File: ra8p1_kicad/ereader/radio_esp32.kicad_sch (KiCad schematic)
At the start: 28 parts, among them U3 ESP32-C6-WROOM-1-N8, U4 TPS22917DBVT, U5 TXU0304PWR, U6 TPS389001DSET, U7 SN74LVC1G97DBVR, U8 SN74LVC1G97DBVR

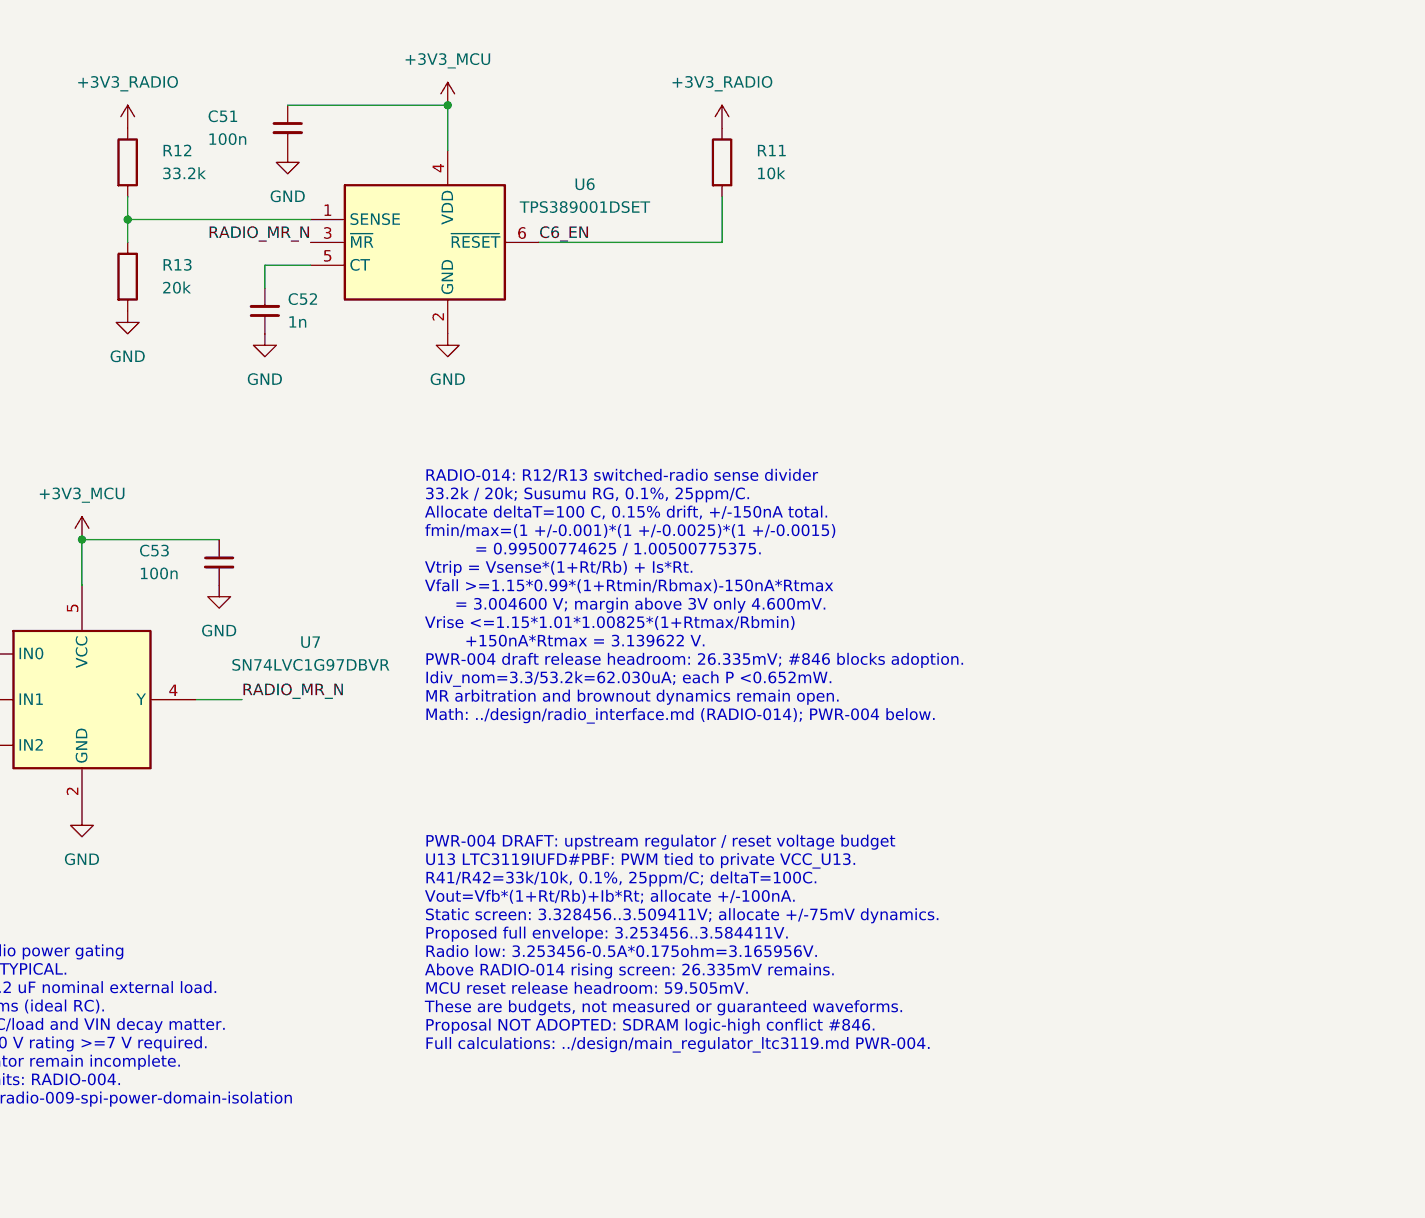
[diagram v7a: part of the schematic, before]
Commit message: Complete MCU reset checkpoint and portable engineering records
Refs #825, #826, #846. Preserve the unresolved radio release margin and unfinished schematic status; refresh full PDF and native BOM.
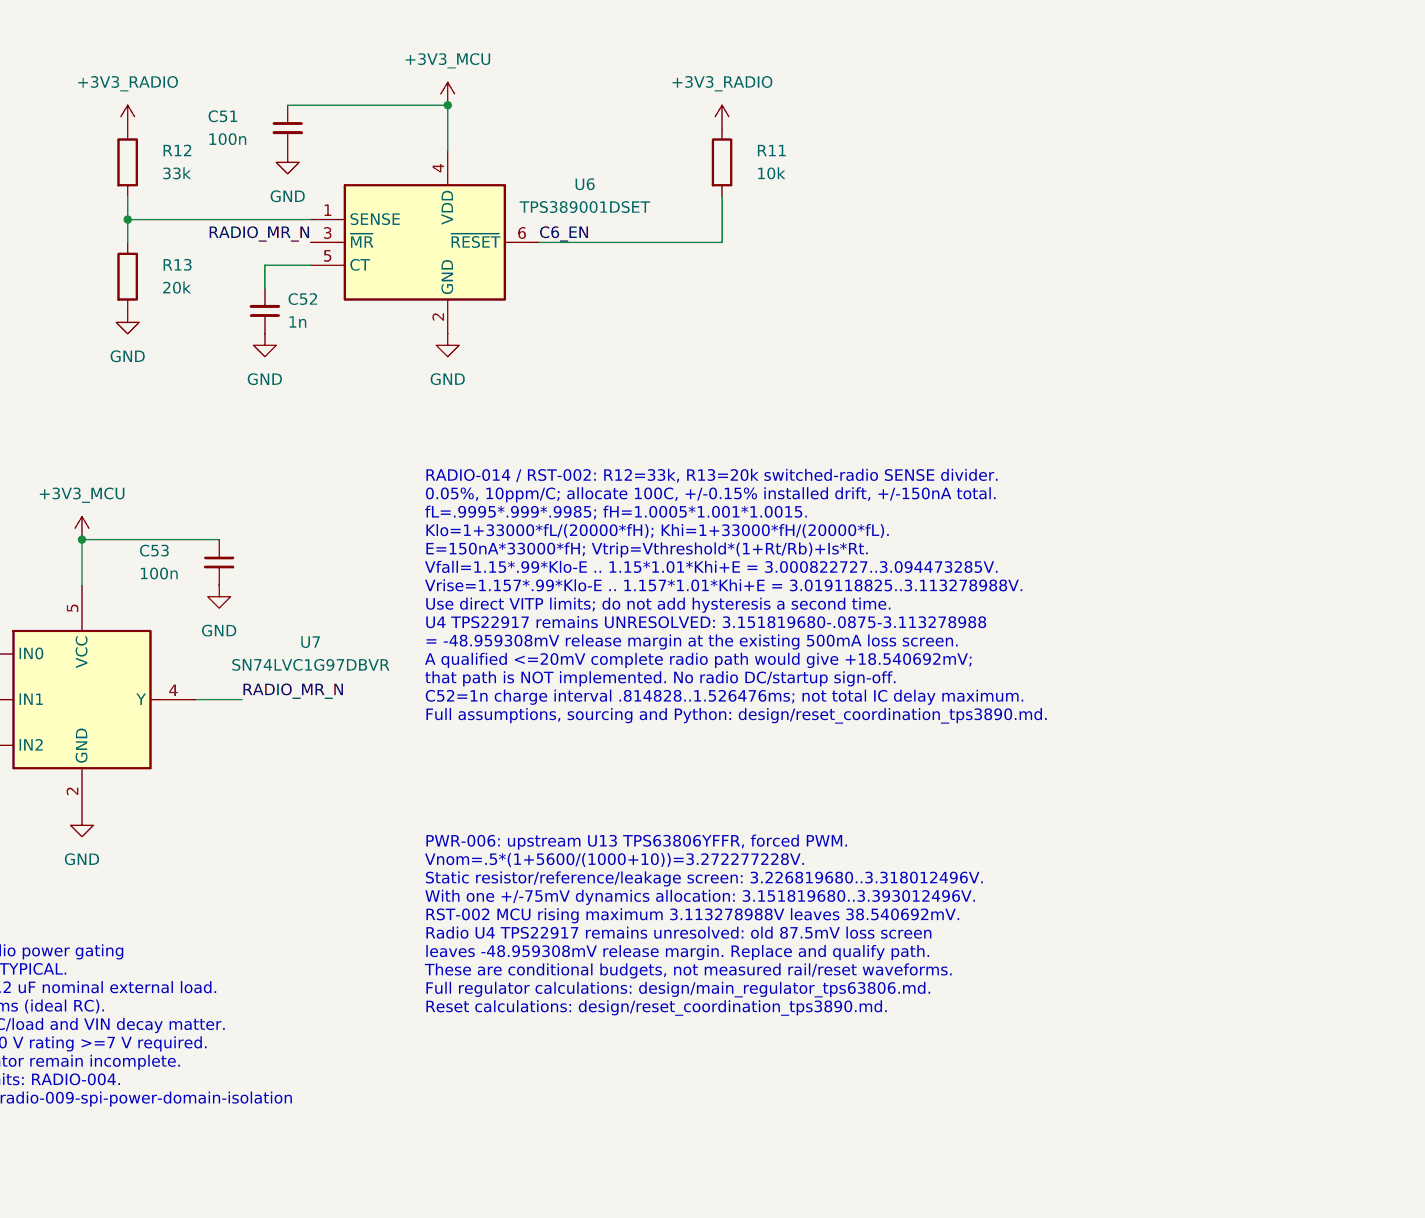
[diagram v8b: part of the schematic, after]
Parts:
- R12: value 33.2k -> 33k; DigiKey_Part_Number RG16P33.2KBCT-ND -> P33KBSCT-ND; DigiKey_URL https://www.digikey.com/en/products/detail/susumu/RG1608P-3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 -> https://www.digikey.com/en/products/detail/panasonic-indust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; Manufacturer_Name Susumu -> Panasonic Industry; Manufacturer_Part_Number RG1608P-3322-B-T5 -> ERA-6ARW333V; Procurement_Status Selected - electrical ratings and sourcing checked; footpri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 -> Selected; installed drift and reset qualification required;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; Selection_Basis RADIO-014 upper divider: 33.2k/20k, 0.1% 25ppm/C. Include 1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 -> RST-002: 33k upper SENSE with 20k lower; 0.05%, 10ppm/C. Co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; Sourcing_Snapshot 2026-09-07 indexed: Active; stock 95362; USD CT 1:0.13 / 10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 -> 2026-09-08 DigiKey cut tape: 9330 stock; USD0.57/0.472/0.39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
- R13: DigiKey_Part_Number RG16P20.0KBCT-ND -> RG16N20.0KWCT-ND; DigiKey_URL https://www.digikey.com/en/products/detail/susumu/RG1608P-2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 -> https://www.digikey.com/en/products/detail/susumu/RG1608N-2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; Manufacturer_Part_Number RG1608P-203-B-T5 -> RG1608N-203-W-T1; Procurement_Status Selected - electrical ratings and sourcing checked; footpri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 -> Selected; installed drift and reset qualification required;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; Selection_Basis RADIO-014 lower divider: 33.2k/20k, 0.1% 25ppm/C. Include 1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 -> RST-002: 20k lower SENSE with 33k upper; 0.05%, 10ppm/C. Co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; Sourcing_Snapshot 2026-09-07 indexed: Active; stock 186950; USD CT 1:0.11 / 1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 -> 2026-09-08 DigiKey cut tape: 78737 stock; USD0.64/0.529/0.4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
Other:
- note added: "PWR-006: upstream U13 TPS63806YFFR, forced PWM. Vnom=.5*(1+5600/(1000+10))=3.272277228V. Static resistor/reference/leakage screen: 3.226819680..3.318012496V. With one +/-75mV dynamics allocation: 3.151819680..3.393012496V. RST-002 MCU rising maximum 3.113278988V leaves 38.540692mV. Radio U4 TPS22917 remains unresolved: old 87.5mV loss screen leaves -48.959308mV release margin. Replace and qualify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"
- note added: "RADIO-014 / RST-002: R12=33k, R13=20k switched-radio SENSE divider. 0.05%, 10ppm/C; allocate 100C, +/-0.15% installed drift, +/-150nA total. fL=.9995*.999*.9985; fH=1.0005*1.001*1.0015. Klo=1+33000*fL/(20000*fH); Khi=1+33000*fH/(20000*fL). E=150nA*33000*fH; Vtrip=Vthreshold*(1+Rt/Rb)+Is*Rt. Vfall=1.15*.99*Klo-E .. 1.15*1.01*Khi+E = 3.000822727..3.094473285V. Vrise=1.157*.99*Klo-E .. 1.157*1.01*Kh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"
- note removed: "PWR-004 DRAFT: upstream regulator / reset voltage budget U13 LTC3119IUFD#PBF: PWM tied to private VCC_U13. R41/R42=33k/10k, 0.1%, 25ppm/C; deltaT=100C. Vout=Vfb*(1+Rt/Rb)+Ib*Rt; allocate +/-100nA. Static screen: 3.328456..3.509411V; allocate +/-75mV dynamics. Proposed full envelope: 3.253456..3.584411V. Radio low: 3.253456-0.5A*0.175ohm=3.165956V. Above RADIO-014 rising screen: 26.335mV remains. 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"
- note removed: "RADIO-014: R12/R13 switched-radio sense divider 33.2k / 20k; Susumu RG, 0.1%, 25ppm/C. Allocate deltaT=100 C, 0.15% drift, +/-150nA total. fmin/max=(1 +/-0.001)*(1 +/-0.0025)*(1 +/-0.0015) = 0.99500774625 / 1.00500775375. Vtrip = Vsense*(1+Rt/Rb) + Is*Rt. Vfall >=1.15*0.99*(1+Rtmin/Rbmax)-150nA*Rtmax = 3.004600 V; margin above 3V only 4.600mV. Vrise <=1.15*1.01*1.00825*(1+Rtmax/Rbmin) +150nA*Rtma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"
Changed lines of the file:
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@@
 		(comment 1 "Incomplete electrical design - not for manufacture")
 	)
-	(text "PWR-004 DRAFT: upstream regulator / reset voltage budget\nU13 LTC3119IUFD#PBF: PWM tied to private VCC_U13.\nR41/R42=33k/10k, 0.1%, 25ppm/C; deltaT=100C.\nVout=Vfb*(1+Rt/Rb)+Ib*Rt; allocate +/-100nA.\nStatic screen: 3.328456..3.509411V; allocate +/-75mV dynamics.\nProposed full envelope: 3.253456..3.584411V.\nRadio low: 3.253456-0.5A*0.175ohm=3.165956V.\nAbove RADIO-014 rising screen: 26.335mV remains.\nMCU reset release headroom: 59.505mV.\nThese are budgets, not measured or guaranteed waveforms.\nProposal NOT ADOPTED: SDRAM logic-high conflict #846.\nFull calculations: ../design/main_regulator_ltc3119.md PWR-004."
+	(text "PWR-006: upstream U13 TPS63806YFFR, forced PWM.\nVnom=.5*(1+5600/(1000+10))=3.272277228V.\nStatic resistor/reference/leakage screen: 3.226819680..3.318012496V.\nWith one +/-75mV dynamics allocation: 3.151819680..3.393012496V.\nRST-002 MCU rising maximum 3.113278988V leaves 38.540692mV.\nRadio U4 TPS22917 remains unresolved: old 87.5mV loss screen\nleaves -48.959308mV release margin. Replace and qualify path.\nThese are conditional budgets, not measured rail/reset waveforms.\nFull regulator calculations: design/main_regulator_tps63806.md.\nReset calculations: design/reset_coordination_tps3890.md."
 		(exclude_from_sim no)
 		(at 266.7 142.24 0)
@@
 			)
 			(justify left top)
-			(href "https://github.com/bsikar/ra8-firmware/blob/design/ereader-circuit/ra8p1_kicad/design/main_regulator_ltc3119.md")
+			(href "https://github.com/bsikar/ra8-firmware/blob/design/ereader-circuit/ra8p1_kicad/design/main_regulator_tps63806.md")
 		)
 	)
@@
 		)
 	)
-	(text "RADIO-014: R12/R13 switched-radio sense divider\n33.2k / 20k; Susumu RG, 0.1%, 25ppm/C.\nAllocate deltaT=100 C, 0.15% drift, +/-150nA total.\nfmin/max=(1 +/-0.001)*(1 +/-0.0025)*(1 +/-0.0015)\n          = 0.99500774625 / 1.00500775375.\nVtrip = Vsense*(1+Rt/Rb) + Is*Rt.\nVfall >=1.15*0.99*(1+Rtmin/Rbmax)-150nA*Rtmax\n      = 3.004600 V; margin above 3V only 4.600mV.\nVrise <=1.15*1.01*1.00825*(1+Rtmax/Rbmin)\n        +150nA*Rtmax = 3.139622 V.\nPWR-004 draft release headroom: 26.335mV; #846 blocks adoption.\nIdiv_nom=3.3/53.2k=62.030uA; each P <0.652mW.\nMR arbitration and brownout dynamics remain open.\nMath: ../design/radio_interface.md (RADIO-014); PWR-004 below."
+	(text "RADIO-014 / RST-002: R12=33k, R13=20k switched-radio SENSE divider.\n0.05%, 10ppm/C; allocate 100C, +/-0.15% installed drift, +/-150nA total.\nfL=.9995*.999*.9985; fH=1.0005*1.001*1.0015.\nKlo=1+33000*fL/(20000*fH); Khi=1+33000*fH/(20000*fL).\nE=150nA*33000*fH; Vtrip=Vthreshold*(1+Rt/Rb)+Is*Rt.\nVfall=1.15*.99*Klo-E .. 1.15*1.01*Khi+E = 3.000822727..3.094473285V.\nVrise=1.157*.99*Klo-E .. 1.157*1.01*Khi+E = 3.019118825..3.113278988V.\nUse direct VITP limits; do not add hysteresis a second time.\nU4 TPS22917 remains UNRESOLVED: 3.151819680-.0875-3.113278988\n= -48.959308mV release margin at the existing 500mA loss screen.\nA qualified <=20mV complete radio path would give +18.540692mV;\nthat path is NOT implemented. No radio DC/startup sign-off.\nC52=1n charge interval .814828..1.526476ms; not total IC delay maximum.\nFull assumptions, sourcing and Python: design/reset_coordination_tps3890.md."
 		(exclude_from_sim no)
 		(at 266.7 101.6 0)
@@
 			)
 			(justify left top)
-			(href "https://github.com/bsikar/ra8-firmware/blob/design/ereader-circuit/ra8p1_kicad/design/radio_interface.md#radio-014-switched-radio-sense-divider")
+			(href "https://github.com/bsikar/ra8-firmware/blob/design/ereader-circuit/ra8p1_kicad/design/reset_coordination_tps3890.md")
 		)
 	)
@@
 			)
 		)
-		(property "Value" "33.2k"
+		(property "Value" "33k"
 			(at 237.49 68.58 0)
 			(show_name no)
@@
 			)
 		)
-		(property "Datasheet" "https://www.susumu.co.jp/dl/?filename=n_catalog_partition01_en.pdf&type=application/pdf"
+		(property "Datasheet" "https://industrial.panasonic.com/jp/products/pt/high-precision-chip-resistors/models/ERA6ARW333V"
 			(at 233.68 67.31 0)
 			(hide yes)
@@
 			)
 		)
-		(property "Description" "Susumu RG1608P-3322-B-T5; 33.2k 0.1% 25ppm/C. RADIO-014 upper SENSE divider from switched +3V3_RADIO to U6.1; full transient qualification open."
+		(property "Description" "33k 0.05% 10ppm/C 0805 thin-film reset sense upper resistor; RST-002"
 			(at 233.68 67.31 0)
 			(hide yes)
@@
 			)
 		)
-		(property "DigiKey_Part_Number" "RG16P33.2KBCT-ND"
+		(property "DigiKey_Part_Number" "P33KBSCT-ND"
 			(at 233.68 67.31 0)
 			(hide yes)
@@
 			)
 		)
-		(property "DigiKey_URL" "https://www.digikey.com/en/products/detail/susumu/RG1608P-3322-B-T5/1240944"
+		(property "DigiKey_URL" "https://www.digikey.com/en/products/detail/panasonic-industry/ERA-6ARW333V/3073417"
 			(at 233.68 67.31 0)
 			(hide yes)
@@
 			)
 		)
-		(property "Procurement_Status" "Selected - electrical ratings and sourcing checked; footprint deferred"
+		(property "Procurement_Status" "Selected; installed drift and reset qualification required; footprint deferred"
 			(at 233.68 67.31 0)
 			(hide yes)
@@
 			)
 		)
-		(property "Sourcing_Snapshot" "2026-09-07 indexed: Active; stock 95362; USD CT 1:0.13 / 10:0.111 / 100:0.09210; 18wk lead; recheck before ordering."
+		(property "Sourcing_Snapshot" "2026-09-08 DigiKey cut tape: 9330 stock; USD0.57/0.472/0.391 at1/10/100; 41wk; unreserved; shipping/tax excluded"
 			(at 233.68 67.31 0)
 			(hide yes)
@@
 			)
 		)
-		(property "Manufacturer_Name" "Susumu"
+		(property "Manufacturer_Name" "Panasonic Industry"
 			(at 233.68 67.31 0)
 			(hide yes)
@@
 			)
 		)
-		(property "Manufacturer_Part_Number" "RG1608P-3322-B-T5"
+		(property "Manufacturer_Part_Number" "ERA-6ARW333V"
 			(at 233.68 67.31 0)
 			(hide yes)
@@
 			)
 		)
-		(property "Selection_Basis" "RADIO-014 upper divider: 33.2k/20k, 0.1% 25ppm/C. Include 100C excursion, 0.15% additional drift and 150nA adverse sense-node current allocations. Falling >=3.004600V; rising <=3.139622V. Static screen only; power/reset dynamics remain open."
+		(property "Selection_Basis" "RST-002: 33k upper SENSE with 20k lower; 0.05%, 10ppm/C. Conditional rising 3.019118825..3.113278988V. See design/reset_coordination_tps3890.md; fast-fault qualification separate."
 			(at 233.68 67.31 0)
 			(hide yes)
@@
 			)
 		)
-		(property "Datasheet" "https://www.susumu.co.jp/dl/?filename=n_catalog_partition01_en.pdf&type=application/pdf"
+		(property "Datasheet" "https://www.susumu.co.jp/common/pdf/n_catalog_partition01_en.pdf"
 			(at 233.68 80.01 0)
 			(hide yes)
@@
 			)
 		)
-		(property "Description" "Susumu RG1608P-203-B-T5; 20k 0.1% 25ppm/C. RADIO-014 lower SENSE divider from U6.1 to GND; full transient qualification open."
+		(property "Description" "20k 0.05% 10ppm/C 0603 thin-film reset sense lower resistor; RST-002"
 			(at 233.68 80.01 0)
 			(hide yes)
@@
 			)
 		)
-		(property "DigiKey_Part_Number" "RG16P20.0KBCT-ND"
+		(property "DigiKey_Part_Number" "RG16N20.0KWCT-ND"
 			(at 233.68 80.01 0)
 			(hide yes)
@@
 			)
 		)
-		(property "DigiKey_URL" "https://www.digikey.com/en/products/detail/susumu/RG1608P-203-B-T5/1240507"
+		(property "DigiKey_URL" "https://www.digikey.com/en/products/detail/susumu/RG1608N-203-W-T1/600628"
 			(at 233.68 80.01 0)
 			(hide yes)
@@
 			)
 		)
-		(property "Procurement_Status" "Selected - electrical ratings and sourcing checked; footprint deferred"
+		(property "Procurement_Status" "Selected; installed drift and reset qualification required; footprint deferred"
 			(at 233.68 80.01 0)
 			(hide yes)
@@
 			)
 		)
-		(property "Sourcing_Snapshot" "2026-09-07 indexed: Active; stock 186950; USD CT 1:0.11 / 10:0.093 / 100:0.07710; 18wk lead; recheck before ordering."
+		(property "Sourcing_Snapshot" "2026-09-08 DigiKey cut tape: 78737 stock; USD0.64/0.529/0.4381 at1/10/100; 22wk; unreserved; shipping/tax excluded"
 			(at 233.68 80.01 0)
 			(hide yes)
@@
 			)
 		)
-		(property "Manufacturer_Part_Number" "RG1608P-203-B-T5"
+		(property "Manufacturer_Part_Number" "RG1608N-203-W-T1"
 			(at 233.68 80.01 0)
 			(hide yes)
@@
 			)
 		)
-		(property "Selection_Basis" "RADIO-014 lower divider: 33.2k/20k, 0.1% 25ppm/C. Include 100C excursion, 0.15% additional drift and 150nA adverse sense-node current allocations. Falling >=3.004600V; rising <=3.139622V. Static screen only; power/reset dynamics remain open."
+		(property "Selection_Basis" "RST-002: 20k lower SENSE with 33k upper; 0.05%, 10ppm/C. Conditional rising 3.019118825..3.113278988V. See design/reset_coordination_tps3890.md; fast-fault qualification separate."
 			(at 233.68 80.01 0)
 			(hide yes)
